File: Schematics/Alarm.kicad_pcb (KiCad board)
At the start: 2 copper layers, 121.9 x 59.7 mm, 7 parts, among them U1 BluetoothModule

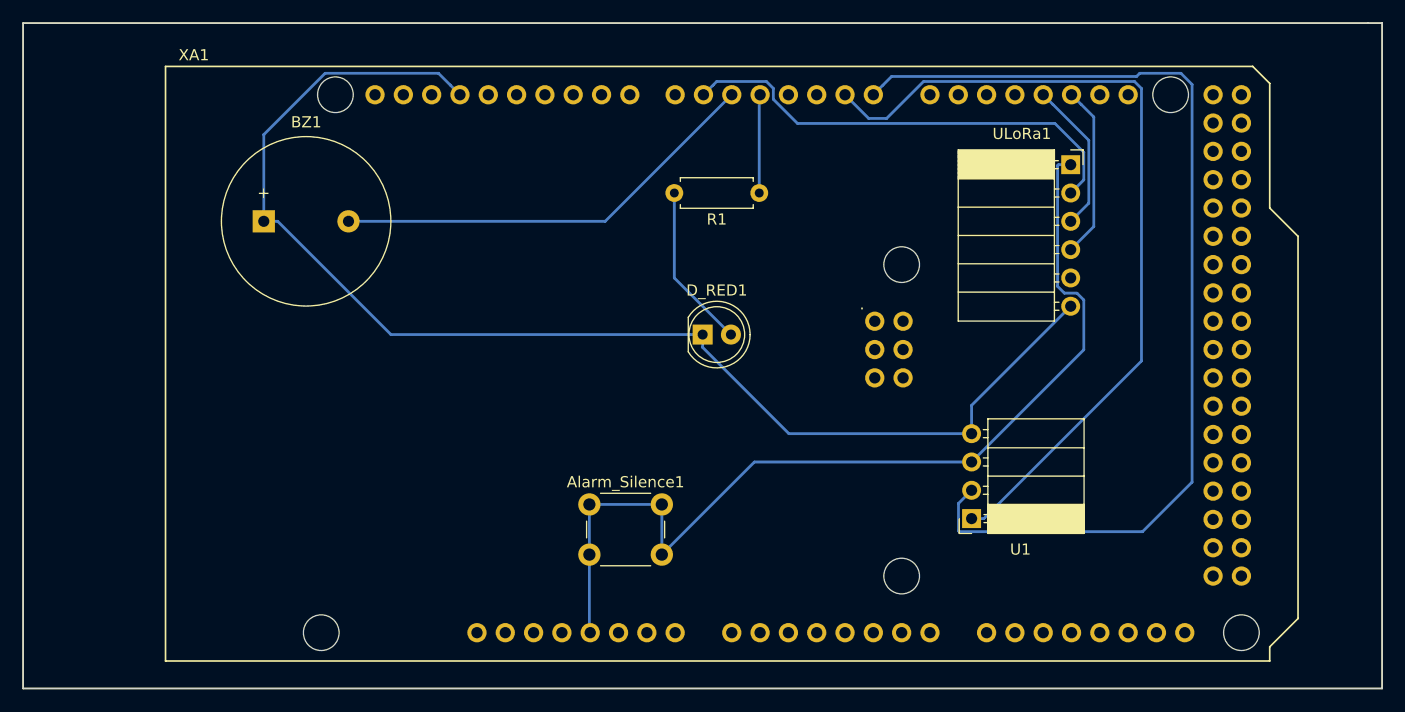
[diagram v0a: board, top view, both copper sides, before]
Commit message: Fixing folder
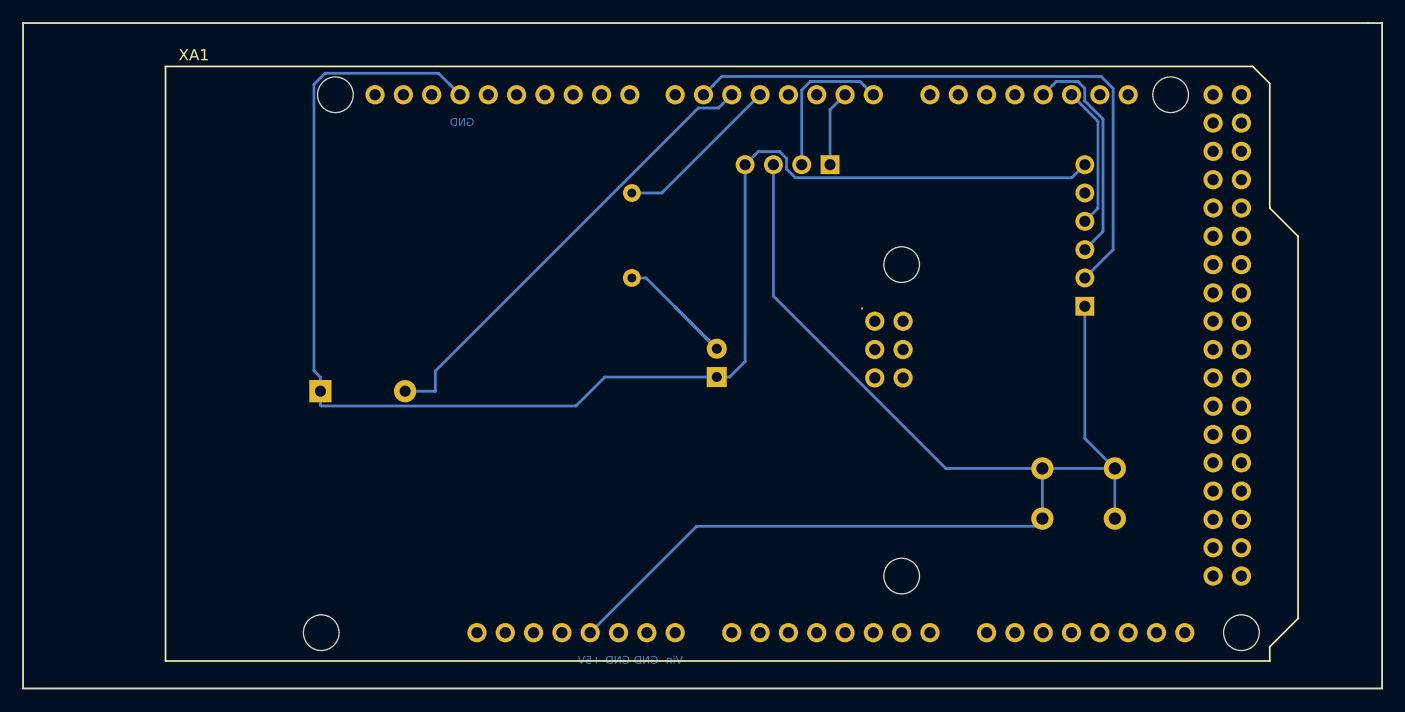
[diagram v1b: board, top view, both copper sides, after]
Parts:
- Alarm_Silence1, BZ1, D_RED1, R1, U1, ULoRa1: moved to B.Cu
- moved Alarm_Silence1 40.7 mm to (168.9, 96.5)
- moved U1 34.2 mm to (149.9, 64.8), turned to 90 degrees
- moved BZ1 16.1 mm to (104.1, 85.1)
- moved ULoRa1 12.8 mm to (172.7, 77.5)
- moved R1 11.4 mm to (132.1, 67.3), turned to 270 degrees
- moved D_RED1 4.02 mm to (139.7, 83.8), turned to 90 degrees
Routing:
- net Net-(U1-Pad2): track 92.4 -> 13.9 mm
- net Net-(U1-Pad1): track 74.7 -> 6.83 mm
- net +5V: track 88.3 -> 120.5 mm
- net GND: track 115.6 -> 133.8 mm
- net Lora_Reset: track 42.0 -> 55.9 mm
- net Net-(ULoRa1-Pad3): track 13.7 -> 20.3 mm
- net Net-(R1-Pad1): track 8.85 -> 15.3 mm
- net Net-(ULoRa1-Pad4): track 15.6 -> 12.8 mm
- net Net-(BZ1-Pad2): track 39.1 -> 41.4 mm
- net Net-(D_RED1-Pad2): track 14.8 -> 15.6 mm
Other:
- board text added: "+5V"
- board text added: "GND"
- board text added: "Vin"
